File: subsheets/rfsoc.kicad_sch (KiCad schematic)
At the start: 1 part, among them U1 nRF54L15-QFXX

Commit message: Added Project-Specific Symbol and Footprint Libraries
Added the NRF54L15 Symbol to the project specific library
(named earworm).  Additional symbols and footprints can be
migrated to these libraries as needed.
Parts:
- U1: symbol PCM_nordic-lib-kicad-nrf54l:nRF54L15-QFXX -> earworm:nRF54L15-QFXX
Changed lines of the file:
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@@
 	(paper "A4")
 	(symbol
-		(lib_id "PCM_nordic-lib-kicad-nrf54l:nRF54L15-QFXX")
+		(lib_id "earworm:nRF54L15-QFXX")
 		(at 147.32 101.6 0)
 		(unit 1)
@@
 		)
 		(property "Footprint" "Package_DFN_QFN:QFN-48-1EP_6x6mm_P0.4mm_EP4.6x4.6mm"
-			(at 147.32 106.68 0)
+			(at 147.32 175.26 0)
 			(effects
 				(font
@@
 		)
 		(property "Datasheet" "https://docs.nordicsemi.com/bundle/ps_nrf54L15"
-			(at 119.38 86.36 0)
+			(at 147.32 177.8 0)
 			(effects
 				(font
@@
 		)
 		(property "Description" "nRF54L Dual Core Multiprotocol BLE SoC"
-			(at 147.32 106.68 0)
+			(at 147.32 172.72 0)
 			(effects
 				(font

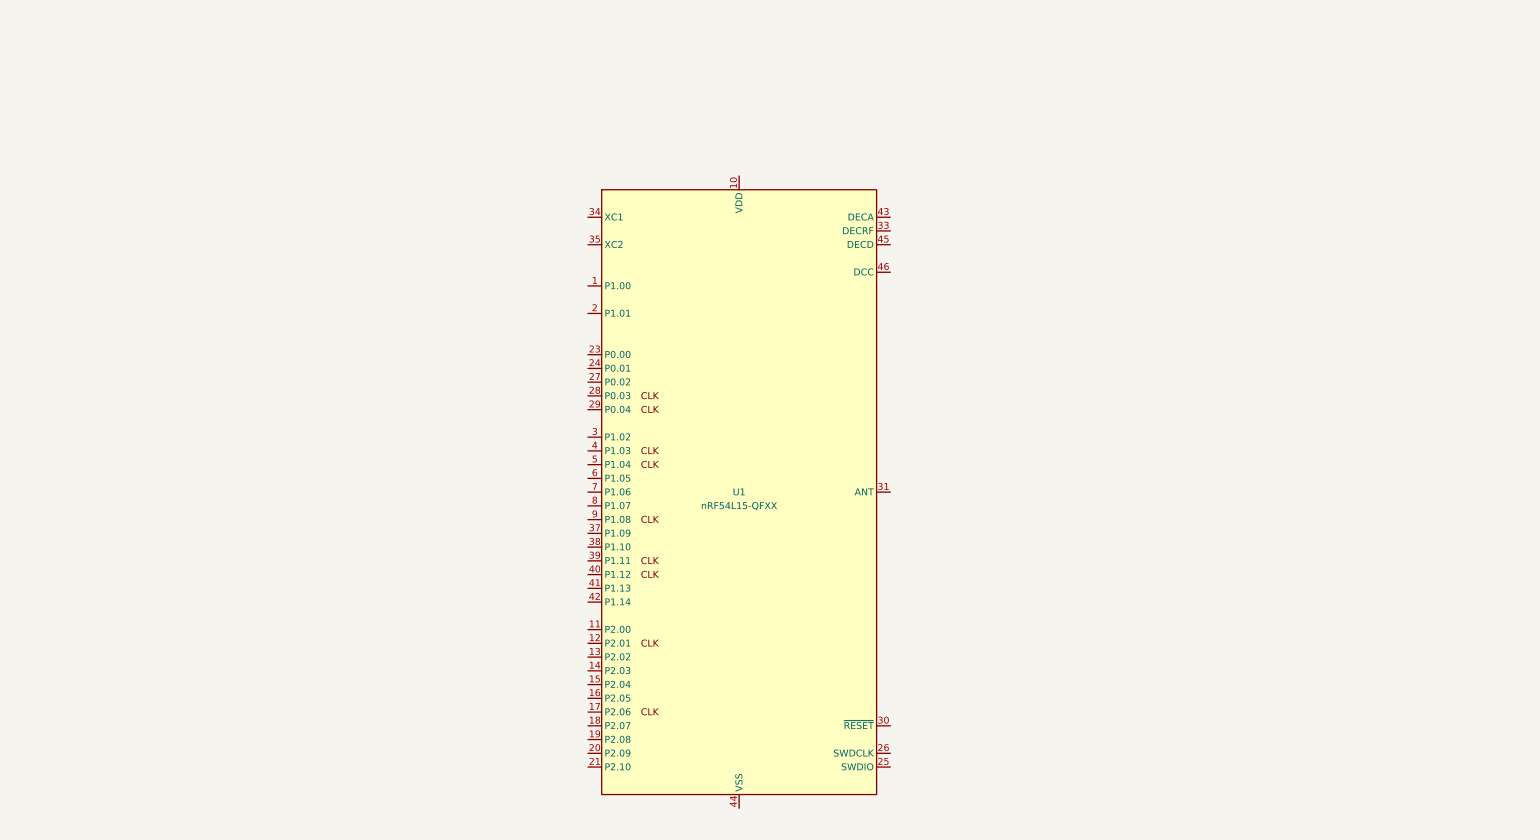
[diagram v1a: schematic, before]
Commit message: Initial MCU schematic. Matches reference nRF54L15 provided by Nordic. Still need to add warnings about phase matching network + additional info
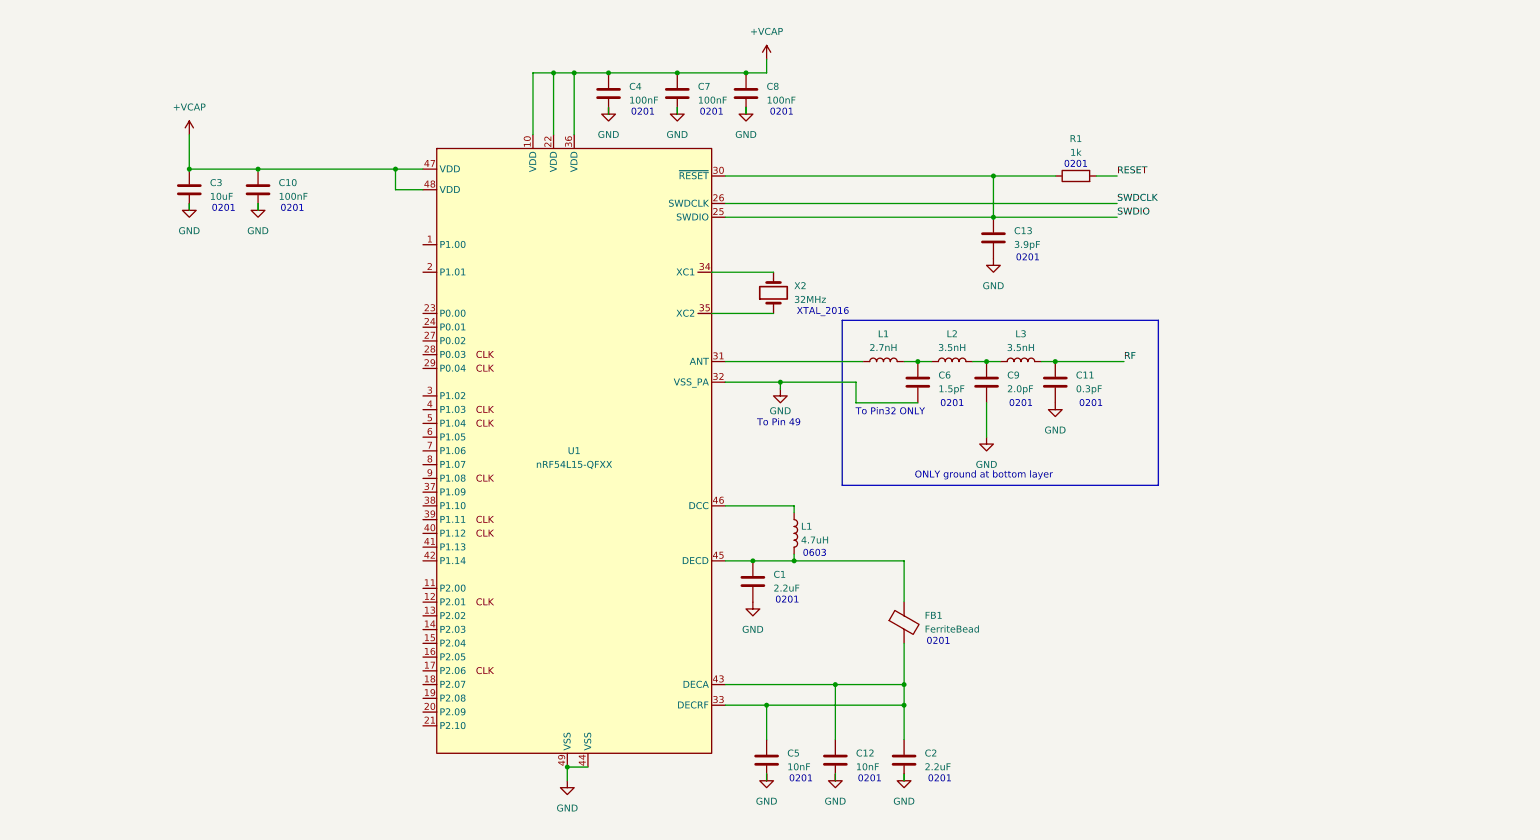
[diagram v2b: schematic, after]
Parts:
- added C1: 2.2uF, symbol Device:C
- added C10, C4, C7, C8: 100nF, 0603, symbol Device:C
- added C11: 0.3pF, 0603, symbol Device:C
- added C12, C5: 10nF, 0603, symbol Device:C
- added C13: 3.9pF, symbol Device:C
- added C2: 2.2uF, 0603, symbol Device:C
- added C3: 10uF, 0603, symbol Device:C
- added C6: 1.5pF, 0603, symbol Device:C
- added C9: 2.0pF, 0603, symbol Device:C
- added FB1: FerriteBead, symbol Device:FerriteBead
- added L1: 2.7nH, symbol Device:L
- added L1: 4.7uH, symbol Device:L
- added L2, L3: 3.5nH, symbol Device:L
- added R1: 1k, symbol Device:R
- added X2: 32MHz, symbol Device:Crystal
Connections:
- net +VCAP: now reaches U1.10 (VDD), U1.22 (VDD), U1.36 (VDD), U1.47 (VDD), U1.48 (VDD)
- net +VCAP: now also C10.1, C3.1, C4.1, C7.1, C8.1
- net SWDIO: now reaches U1.25 (SWDIO)
- net SWDIO: now also U1.30 (~{RESET}), C13.1, R1.1
- net SWDCLK: now reaches U1.26 (SWDCLK)
- net at U1.31 (ANT): now also L1.1
- net GND: now reaches U1.32 (VSS_PA), U1.44 (VSS), U1.49 (VSS)
- net GND: now also C1.2, C10.2, C11.2, C12.2, C13.2, C2.2, C3.2, C4.2, C5.2, C6.2, C7.2, C8.2, C9.2
- net at U1.33 (DECRF): now also U1.43 (DECA), C12.1, C2.1, C5.1, FB1.2
- net at U1.34 (XC1): now also X2.2
- net at U1.35 (XC2): now also X2.1
- net at U1.45 (DECD): now also C1.1, FB1.1, L1.2
- net at U1.46 (DCC): now also L1.1
- new net: C6.1, L1.2, L2.1
- new net: C9.1, L2.2, L3.1
- new net RESET: R1.2
- new net RF: C11.1, L3.2
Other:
- note added: "0201"
- note added: "0603"
- note added: "ONLY ground at bottom layer"
- note added: "To Pin 49"
- note added: "To Pin32 ONLY"
- note added: "XTAL_2016"

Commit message: RFSoC schematic almost complete. Still need to determine filtering for ADXL367
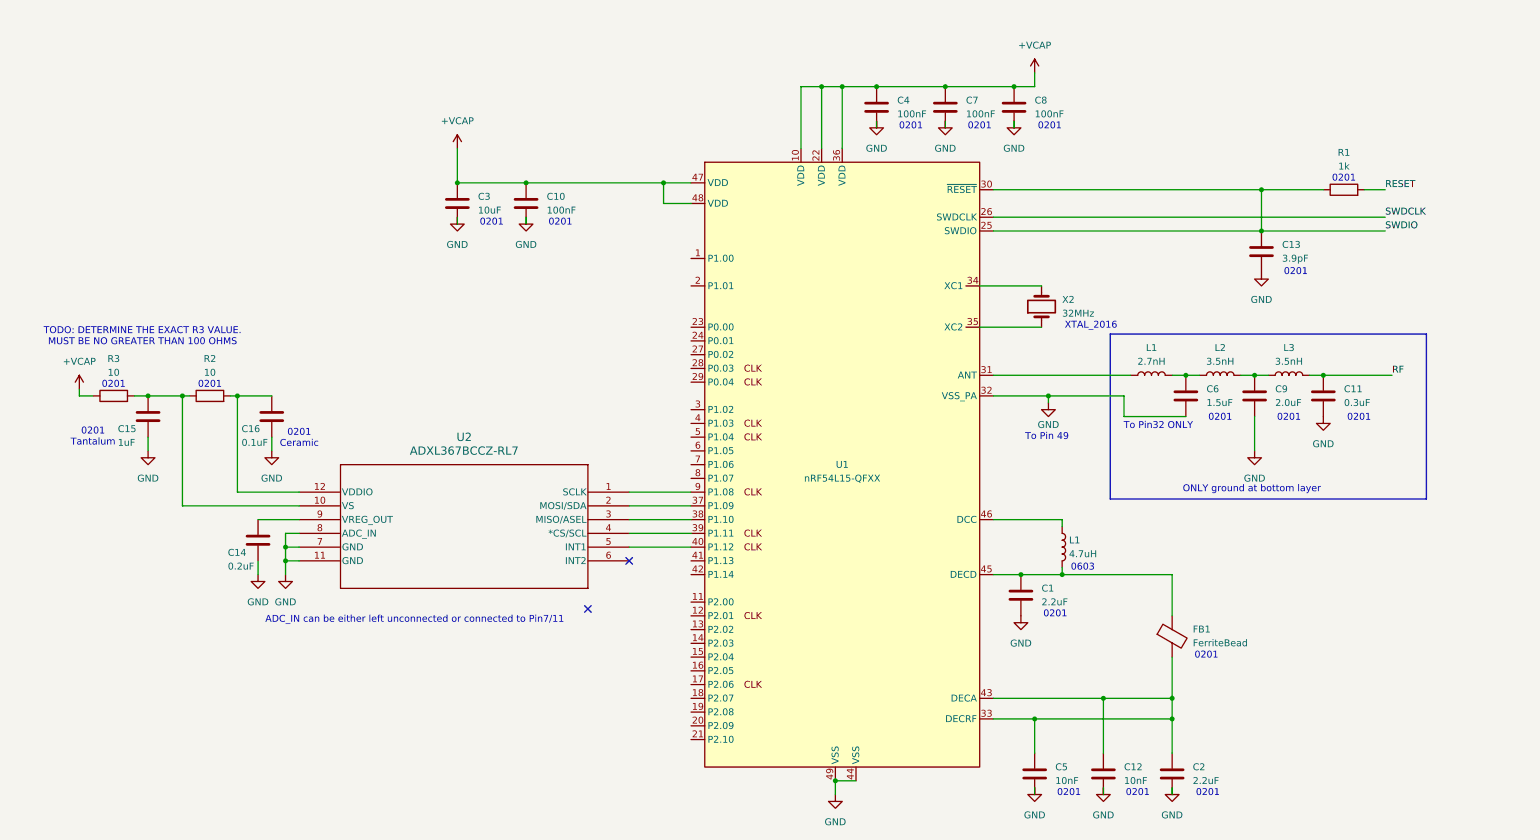
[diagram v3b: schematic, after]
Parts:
- added C14: 0.2uF, symbol Device:C
- added C15: 1uF, symbol Device:C
- added C16: 0.1uF, symbol Device:C
- added R2, R3: 10, symbol Device:R
- added U2: ADXL367BCCZ-RL7, symbol earworm:ADXL367BCCZ-RL7
- C11: value 0.3pF -> 0.3uF
- C6: value 1.5pF -> 1.5uF
- C9: value 2.0pF -> 2.0uF
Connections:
- net +VCAP: now also R3.1
- net GND: now also C14.2, C15.2, C16.2, U2.11 (GND), U2.7 (GND), U2.8 (ADC_IN)
- net at U1.37 (P1.09): now also U2.2 (MOSI/SDA)
- net at U1.38 (P1.10): now also U2.3 (MISO/ASEL)
- net at U1.39 (P1.11): now also U2.4 (*CS/SCL)
- net at U1.40 (P1.12): now also U2.5 (INT1)
- net at U1.9 (P1.08): now also U2.1 (SCLK)
- new net: C16.1, R2.2, U2.12 (VDDIO)
- new net: C14.1, U2.9 (VREG_OUT)
- new net: C15.1, R2.1, R3.2, U2.10 (VS)
- no-connect marks 0 -> 2
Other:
- note added: "0201 Ceramic"
- note added: "0201 Tantalum"
- note added: "ADC_IN can be either left unconnected or connected to Pin7/11"
- note added: "TODO: DETERMINE THE EXACT R3 VALUE. MUST BE NO GREATER THAN 100 OHMS"
- moved on the sheet: C1, C10, C11, C12, C13, C2, C3, C4, C5, C6, C7, C8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

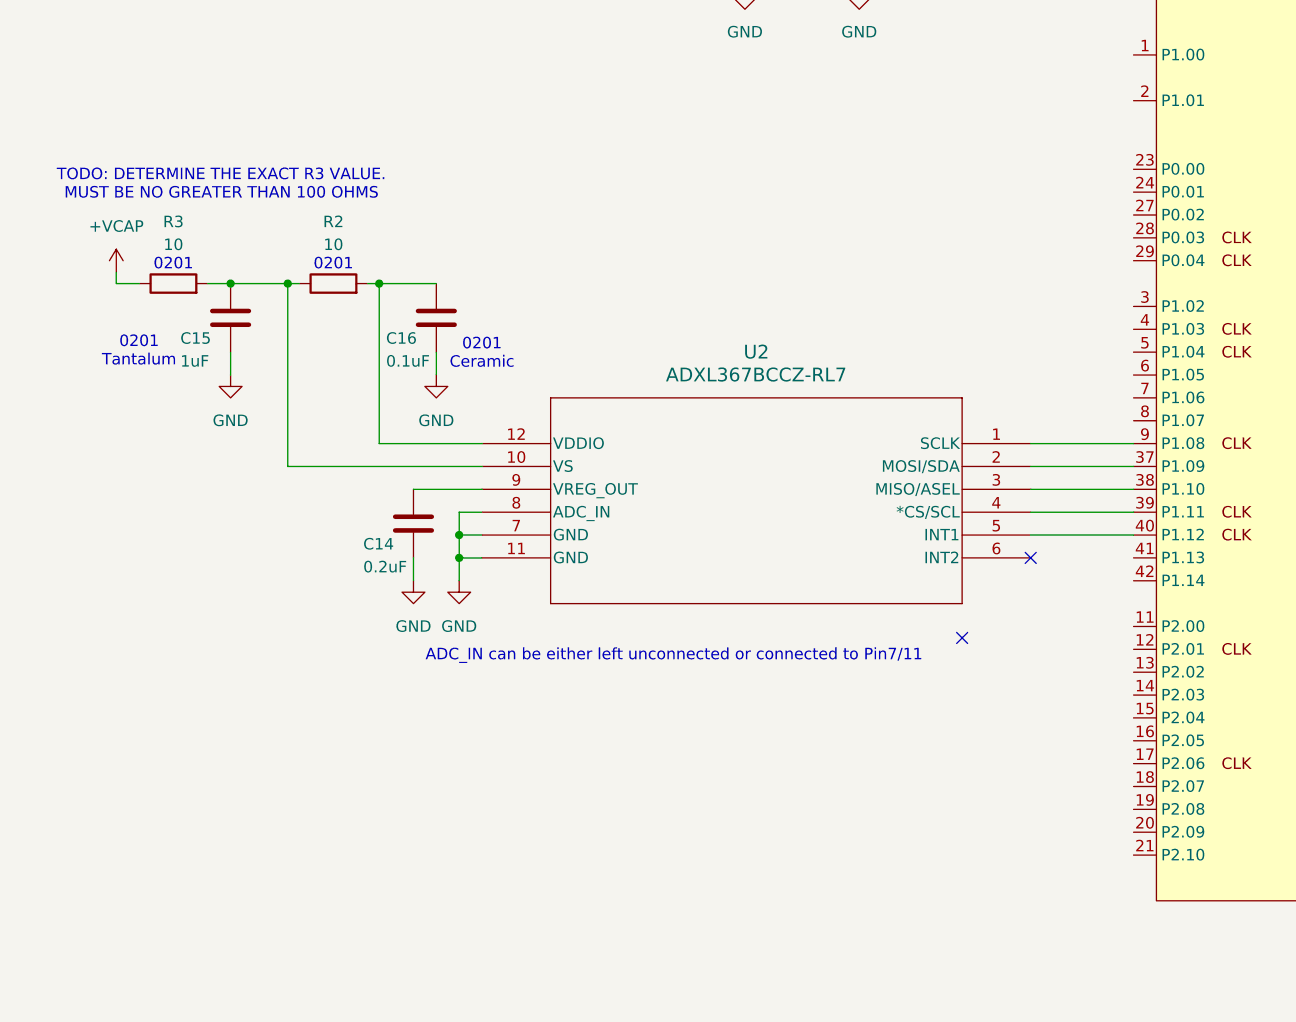
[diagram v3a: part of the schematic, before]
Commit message: Changed ADXL367 to work with proper pins in port 2
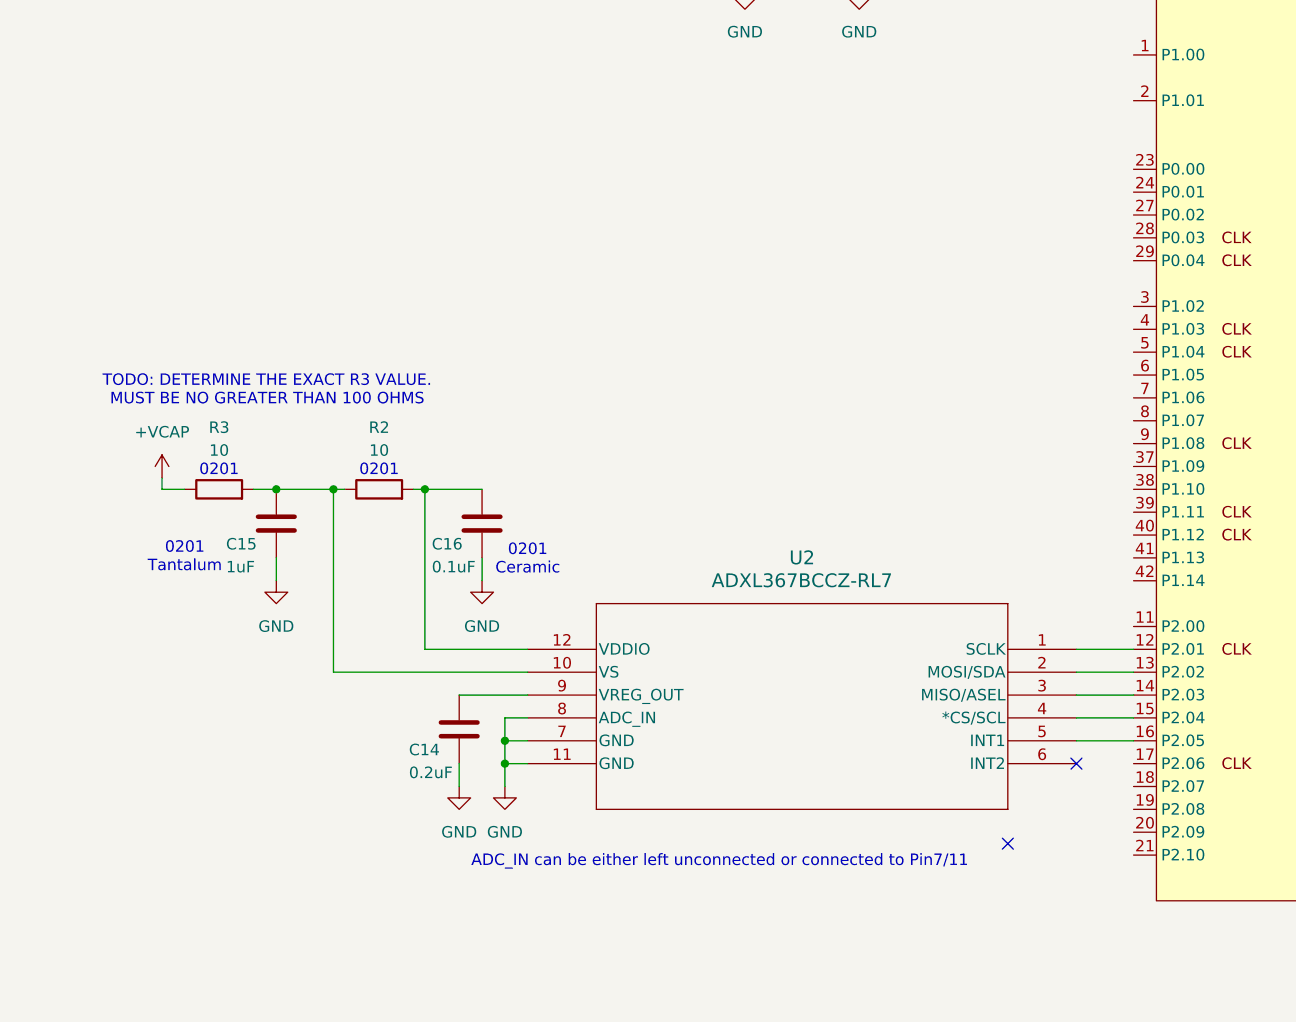
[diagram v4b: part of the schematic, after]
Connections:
- net at U2.1 (SCLK): now also U1.12 (P2.01); no longer U1.9 (P1.08)
- net at U2.2 (MOSI/SDA): now also U1.13 (P2.02); no longer U1.37 (P1.09)
- net at U2.3 (MISO/ASEL): now also U1.14 (P2.03); no longer U1.38 (P1.10)
- net at U2.4 (*CS/SCL): now also U1.15 (P2.04); no longer U1.39 (P1.11)
- net at U2.5 (INT1): now also U1.16 (P2.05); no longer U1.40 (P1.12)
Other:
- moved on the sheet: C14, C15, C16, R2, R3, U2
